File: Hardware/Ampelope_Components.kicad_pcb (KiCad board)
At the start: 4 copper layers, 60.5 x 81.6 mm, 123 parts, among them J1 Conn_01x12_Male, J2 Conn_01x12_Male, J3 Conn_01x12_Male, J4 Conn_01x12_Male, J5 Eurorack_16_pin_power, J6 Conn_01x02_Male, J7 SWD_Header, J8 USB_B_Micro, J9 Conn_01x02_Male, Q1 MMBT3904, Q2 MMBT3904, Q3 MMBT3904, Q4 MMBT3904, Q5 MMBT3904, U1 STM32G431RB, U2 AS3364, U3 LM1117-3.3, U4 TL074, U5 TL074, U6 TL074, Y1 8MHz 20pF

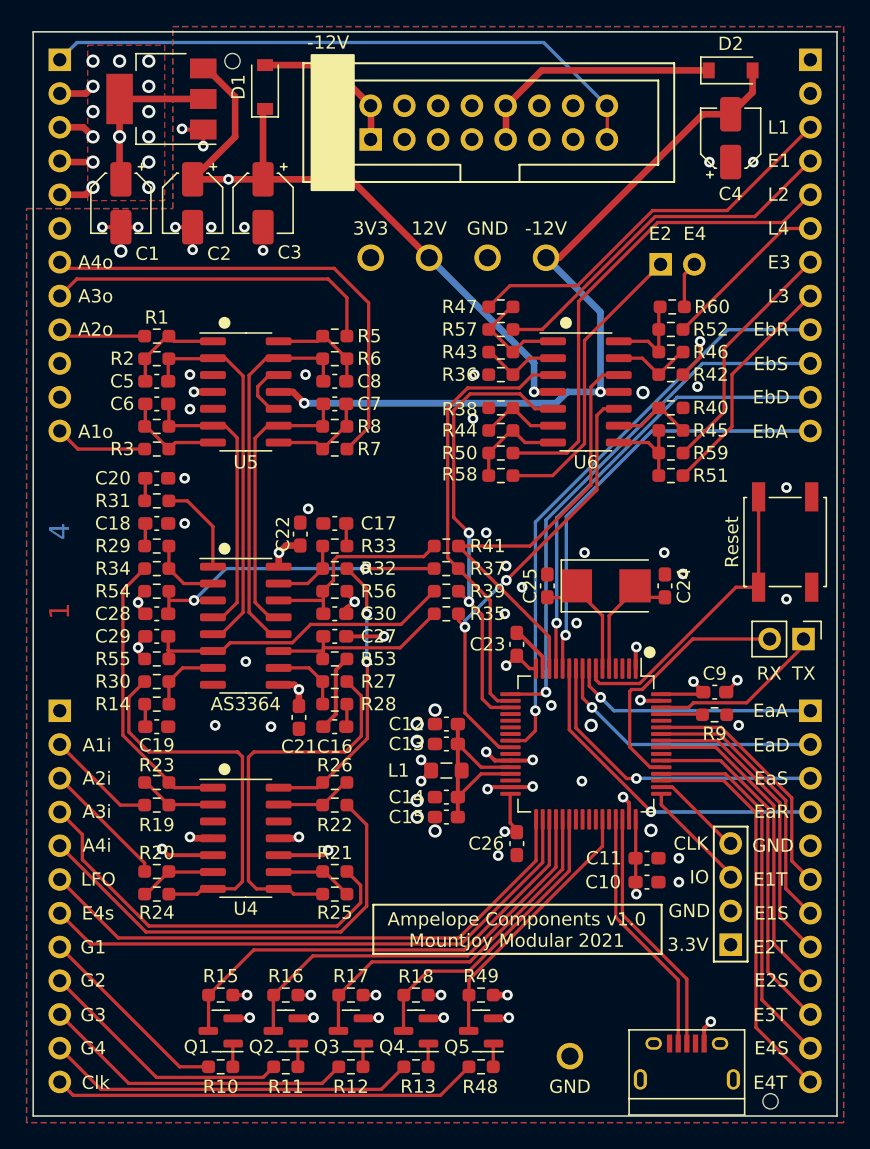
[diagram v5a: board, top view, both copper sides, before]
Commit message: Fixes to component schematic and pcb (power supply and silkscreen); Firmware updated to use correct pin assignments
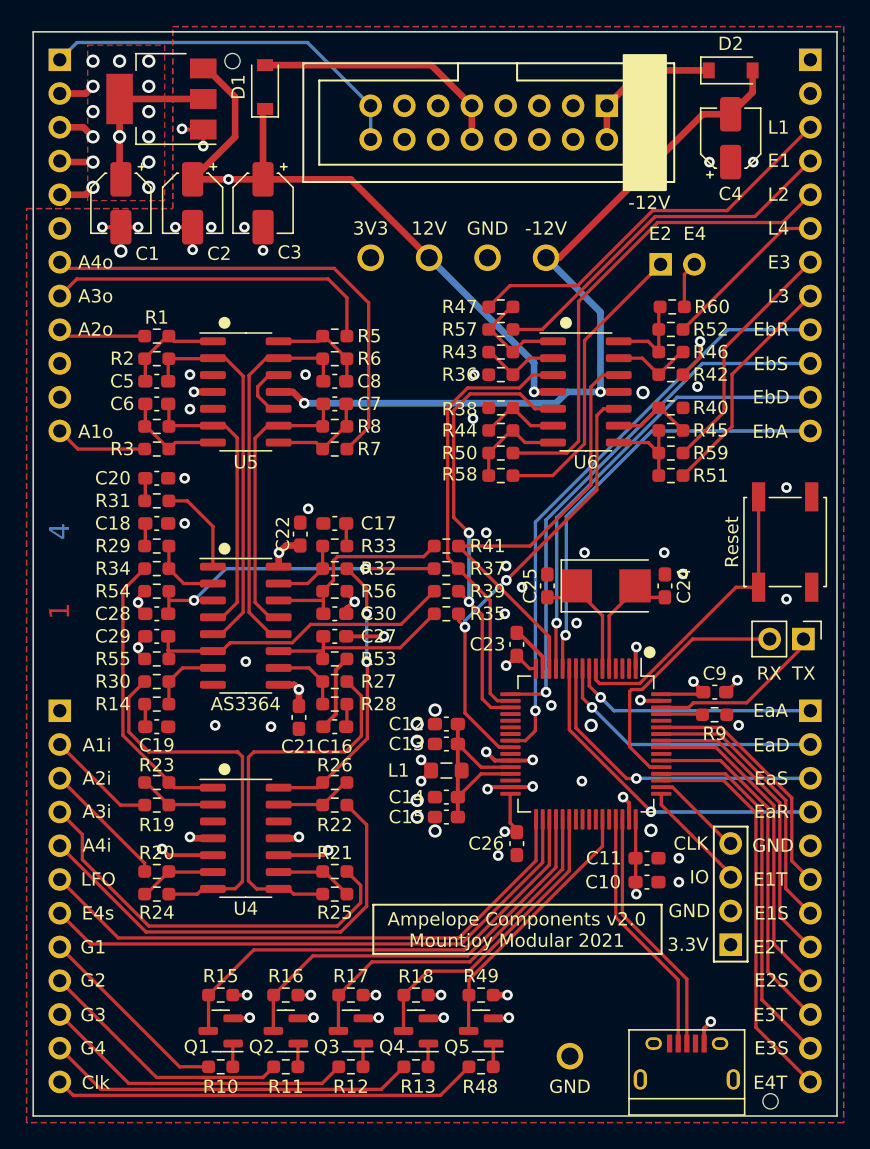
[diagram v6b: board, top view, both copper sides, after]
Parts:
- moved J5 18.0 mm to (143.2, 55.6), turned to 180 degrees
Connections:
- J5 pad 1: +12V -> -12V
- J5 pad 10: -12V -> +12V
- J5 pad 2: +12V -> -12V
- J5 pad 9: -12V -> +12V
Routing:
- net /Gate_In: track 46.3 -> 28.5 mm
- net -12V: track 18.9 -> 11.3 mm
- net +12V: track 11.8 -> 19.4 mm
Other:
- board text added: "Ampelope Components v2.0 Mountjoy Modular 2021"
- board text added: "E3S"
- board text removed: "Ampelope Components v1.0 Mountjoy Modular 2021"
- board text removed: "E4S"
